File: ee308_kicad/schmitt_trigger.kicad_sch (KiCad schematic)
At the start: 0 parts

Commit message: Update Schmitt schematic, update Schmitt simulation values.
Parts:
- added C13: 56p, Capacitor_SMD:C_0805_2012Metric_Pad1.18x1.45mm_HandSolder, symbol Device:C
- added C14, C15: 0.1u, Capacitor_SMD:C_0805_2012Metric_Pad1.18x1.45mm_HandSolder, symbol Device:C
- added D10, D11, D12, D13, D14, D15, D16, D3, D4, D5, D6, D7, D8, D9: 1N6263, Diode_THT:D_DO-35_SOD27_P7.62mm_Horizontal, symbol Diode:1N6263
- added Q10, Q8, Q9: 2N3904, Package_TO_SOT_THT:TO-92_Inline, symbol Transistor_BJT:2N3904
- added Q11, Q12: 2N3906, Package_TO_SOT_THT:TO-92_Inline, symbol Transistor_BJT:2N3906
- added R16, R17, R18: 1k, Resistor_SMD:R_0805_2012Metric_Pad1.20x1.40mm_HandSolder, symbol Device:R_US
- added R19, R20: 1.6k, Resistor_SMD:R_0805_2012Metric_Pad1.20x1.40mm_HandSolder, symbol Device:R_US
- added R21: 910, Resistor_SMD:R_0805_2012Metric_Pad1.20x1.40mm_HandSolder, symbol Device:R_US
- added R22, R23: 2.5k, Resistor_SMD:R_0805_2012Metric_Pad1.20x1.40mm_HandSolder, symbol Device:R_US
- added R24, R25: 6.5k, Resistor_SMD:R_0805_2012Metric_Pad1.20x1.40mm_HandSolder, symbol Device:R_US
- added RV3, RV5: 10k, Potentiometer_SMD:Potentiometer_ACP_CA6-VSMD_Vertical, symbol Device:R_Potentiometer_US
- added RV4: 100k, symbol Device:R_Potentiometer_US
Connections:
- new net: D10.1 (K), D11.2 (A), D14.1 (K), D16.2 (A), Q11.3 (C), R22.1
- new net: Q11.1 (E), Q12.1 (E), R21.2
- new net: D7.1 (K), D8.2 (A)
- new net: D13.2 (A), D14.2 (A), R24.2
- new net: D15.1 (K), D16.1 (K), R25.1
- new net: R25.2, RV5.1
- new net: D5.2 (A), D6.1 (K)
- new net: D3.1 (K), D4.2 (A), Q11.2 (B), Q9.3 (C), R20.2
- new net: D3.2 (A), D4.1 (K), Q8.3 (C), R19.2
- new net: R24.1, RV3.3
- new net: D11.1 (K), D12.2 (A)
- new net: Q10.1 (E), R18.1
- new net: Q10.3 (C), Q8.1 (E), Q9.1 (E)
- new net: C13.2, Q8.2 (B), R16.2, R17.1
- new net: D13.1 (K), D15.2 (A), Q9.2 (B)
- new net: D10.2 (A), D9.1 (K)
- new net: Q10.2 (B), RV4.2
- new net +12V: C14.2, R19.1, R20.1, R21.1, RV3.1, RV3.2
- new net -12V: C15.1, R18.2, R22.2, R23.2, RV4.3, RV5.2, RV5.3
- new net GND: C14.1, C15.2, D12.1 (K), D6.2 (A), D8.1 (K), D9.2 (A), R17.2, RV4.1
- new net schmitt_in: C13.1, R16.1
- new net square_out: D5.1 (K), D7.2 (A), Q12.3 (C), R23.1

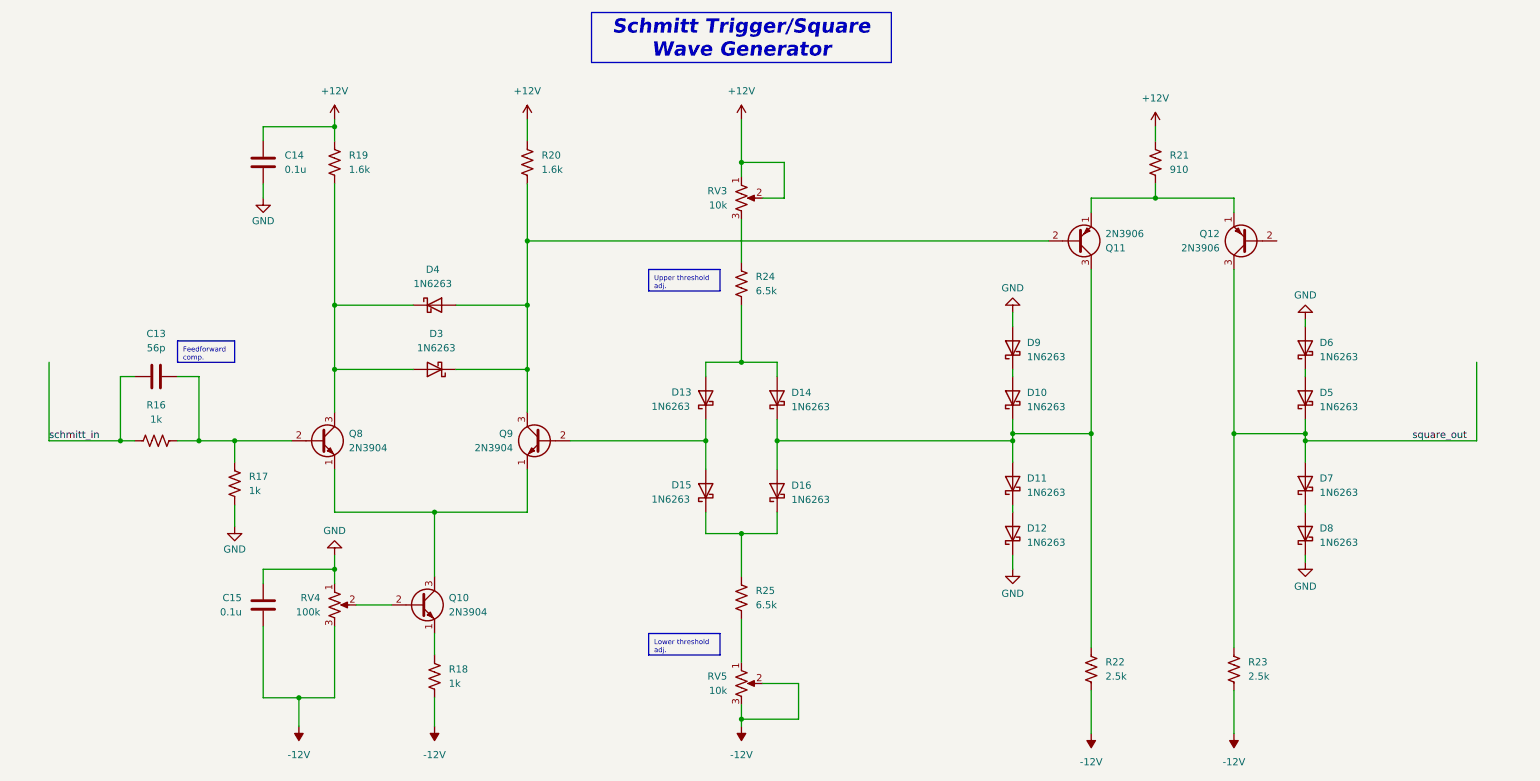
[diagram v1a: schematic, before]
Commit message: Update with current switch/integrator.
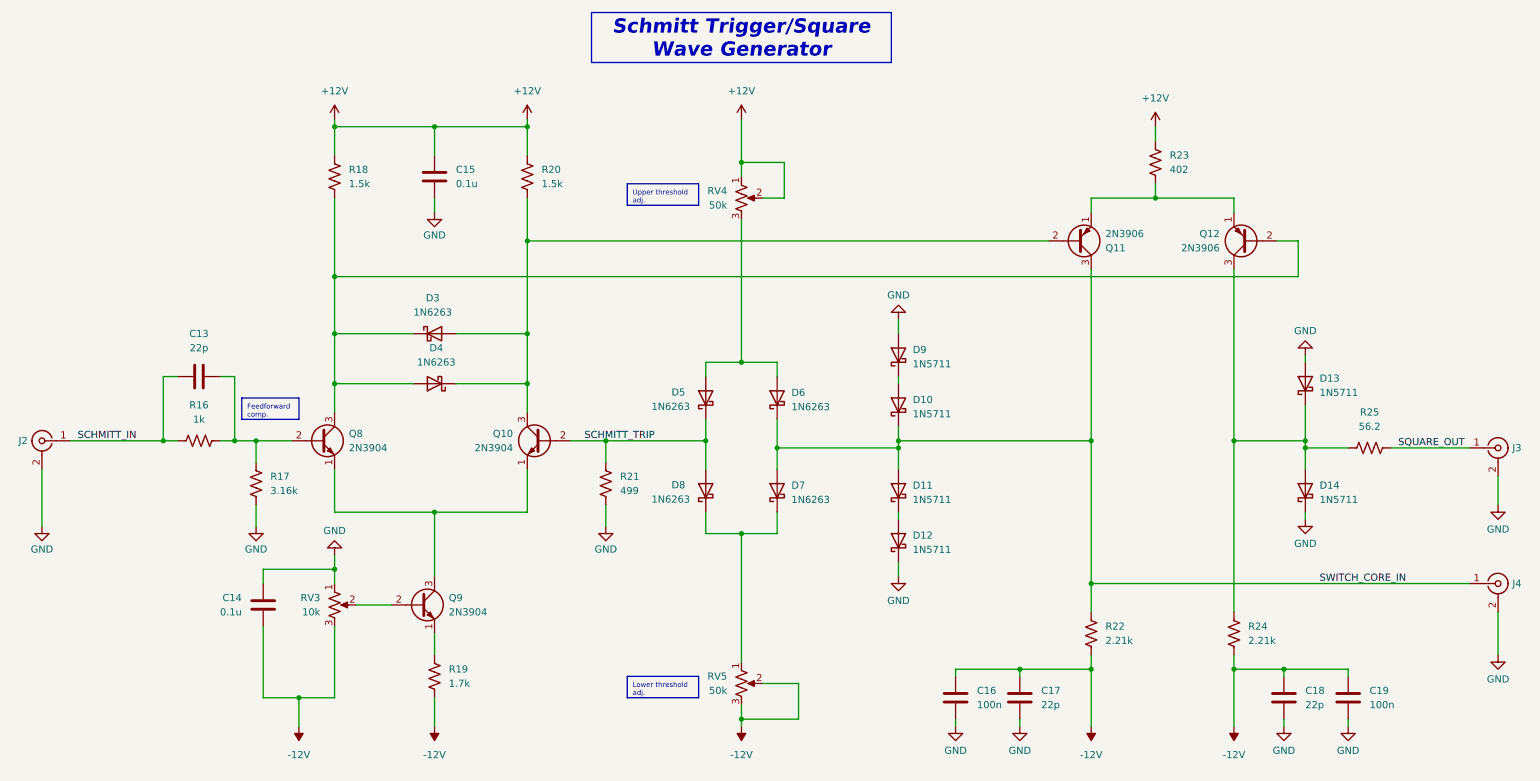
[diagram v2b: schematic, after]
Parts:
- removed D10, D11, D12, D5, D6, D7, D8, D9: 1N6263, Diode_THT:D_DO-35_SOD27_P7.62mm_Horizontal, symbol Diode:1N6263
- removed R24: 6.5k, Resistor_SMD:R_0805_2012Metric_Pad1.20x1.40mm_HandSolder, symbol Device:R_US
- added C16, C19: 100n, Capacitor_SMD:C_0805_2012Metric_Pad1.18x1.45mm_HandSolder, symbol Device:C
- added C17, C18: 22p, Capacitor_SMD:C_0805_2012Metric_Pad1.18x1.45mm_HandSolder, symbol Device:C
- added D10, D11, D12, D13, D14, D9: 1N5711, Diode_THT:D_DO-35_SOD27_P7.62mm_Horizontal, symbol Diode:1N5711
- added J2, J3, J4: Conn_Coaxial, Connector_Coaxial:SMA_Amphenol_901-143_Horizontal, symbol Connector:Conn_Coaxial
- added R21: 499, Resistor_SMD:R_0805_2012Metric_Pad1.20x1.40mm_HandSolder, symbol Device:R_US
- C13: value 56p -> 22p
- R17: value 1k -> 3.16k
- R18: renamed from R19; value 1.6k -> 1.5k
- R19: renamed from R18; value 1k -> 1.7k
- R20: value 1.6k -> 1.5k
- R22: value 2.5k -> 2.21k
- R23: renamed from R21; value 910 -> 402
- R24: renamed from R23; value 2.5k -> 2.21k
- R25: value 6.5k -> 56.2
- RV3: renamed from RV4; value 100k -> 10k
- RV4: renamed from RV3; value 10k -> 50k
- RV5: value 10k -> 50k
- renumbered C15 to C14, C14 to C15, D4 to D3, D3 to D4, D13 to D5, D14 to D6, D16 to D7, D15 to D8, Q9 to Q10, Q10 to Q9
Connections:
- net -12V: now also C16.2, C17.2, C18.2, C19.2
- net GND: now also C16.1, C17.1, C18.1, C19.1, D12.1 (K), D13.2 (A), D14.1 (K), D9.2 (A), J2.2 (Ext), J3.2 (Ext), J4.2 (Ext), R21.2
- net SWITCH_CORE_IN: now reaches D6.1 (K), D7.2 (A), Q11.3 (C), R22.1
- net SWITCH_CORE_IN: now also D10.1 (K), D11.2 (A), J4.1 (In)
- net at D5.2 (A), D6.2 (A): now also RV4.3
- net at D7.1 (K), D8.1 (K): now also RV5.1; no longer R25.1
- net SQUARE_OUT: now reaches R25.2
- net SQUARE_OUT: now also J3.1 (In); no longer RV5.1
- net at D3.1 (K), D4.2 (A), Q8.3 (C)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: now also Q12.2 (B)
- net SCHMITT_TRIP: now reaches D5.1 (K), D8.2 (A), Q10.2 (B)
- net SCHMITT_TRIP: now also R21.1
- net schmitt_in renamed SCHMITT_IN
- net SCHMITT_IN: now also J2.1 (In)
- net square_out: no longer names the net of Q12.3 (C), R24.1
- net square_out: now also R25.1, D13.1 (K), D14.2 (A)
- new net: D11.1 (K), D12.2 (A)
- new net: D10.2 (A), D9.1 (K)
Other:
- moved on the sheet: C13, C15, D3, D4, R16, R17, R18, R20, R22, R24
